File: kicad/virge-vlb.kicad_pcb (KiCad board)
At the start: 4 copper layers, 240.5 x 69.4 mm, 92 parts, among them J1 VLB_slot, J2 VGA, U1 74LS244, U2 27C020, U7 86C325, U8 7404, U9 7408, Y1 14.318MHz

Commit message: changed QFP and ROM footprint
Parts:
- added REF**: PLCC-28_SMD-Socket, Package_LCC:PLCC-28_SMD-Socket, F.Cu at (128.2, 170.0)
- added REF**: PLCC-32_11.4x14.0mm_P1.27mm, Package_LCC:PLCC-32_11.4x14.0mm_P1.27mm, F.Cu at (145.7, 170.3)
- J2: footprint Connector_Dsub:DSUB-15-HD_Female_Horizontal_P2.29x1.98mm_EdgePinOffset8.35mm_Housed_MountingHolesOffset10.89mm -> VLB:DSUB-15_female
- R22: value 33R -> 2 x 33R
- U2: footprint Package_DIP:DIP-32_W15.24mm -> VLB:EEPROM_combo
- U7: footprint Package_QFP:PQFP-208_28x28mm_P0.5mm -> VLB:QFP-208
- moved R6 42.0 mm to (191.2, 132.7)
- moved U2 41.2 mm to (187.4, 130.4), turned to 90 degrees
- moved R7 38.3 mm to (189.7, 112.8), turned to 180 degrees
- moved C9 12.1 mm to (231.2, 118.8)
- moved C20 4.72 mm to (254.2, 130.3)
- moved U7 2.49 mm to (97.6, 115.2)
- moved R46 1.50 mm to (74.8, 130.8)
- moved R48 1.48 mm to (76.8, 130.8)
- moved R47 1.47 mm to (75.8, 127.9)
- moved U1 1.45 mm to (239.2, 122.7), turned to 90 degrees
- moved R22 0.45 mm to (99.2, 96.0)
- moved R21 0.44 mm to (97.2, 96.0)
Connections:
- U1 pad 12: /ISA Bus/R_D4 -> /ISA Bus/R_D7
- U1 pad 14: /ISA Bus/R_D5 -> /ISA Bus/R_D6
- U1 pad 16: /ISA Bus/R_D6 -> /ISA Bus/R_D5
- U1 pad 18: /ISA Bus/R_D7 -> /ISA Bus/R_D4
- U1 pad 2: /ISA Bus/ISA_D7 -> /ISA Bus/ISA_D4
- U1 pad 4: /ISA Bus/ISA_D6 -> /ISA Bus/ISA_D5
- U1 pad 6: /ISA Bus/ISA_D5 -> /ISA Bus/ISA_D6
- U1 pad 8: /ISA Bus/ISA_D4 -> /ISA Bus/ISA_D7
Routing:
- net /ISA Bus/R_D0: track 86.5 -> 28.3 mm, vias 0 -> 1
- net /ISA Bus/R_D1: track 74.5 -> 30.0 mm, vias 0 -> 1
- net /ISA Bus/R_A10: track 14.4 -> 58.6 mm, vias 0 -> 1
- net /ISA Bus/R_A11: track 16.2 -> 52.3 mm, vias 0 -> 1
- net /ISA Bus/R_D2: track 63.2 -> 33.3 mm, vias 0 -> 1
- net /ISA Bus/R_A9: track 27.1 -> 50.9 mm, vias 0 -> 1
- net /ISA Bus/R_D3: track 62.6 -> 39.7 mm, vias 0 -> 1
- net /ISA Bus/R_D4: track 48.9 -> 28.3 mm
- net /ISA Bus/R_A0: track 40.3 -> 60.1 mm, vias 0 -> 2
- net /ISA Bus/R_A14: track 18.9 -> 37.7 mm, vias 0 -> 2
- net /ISA Bus/R_A12: track 36.3 -> 18.9 mm, vias 2 -> 0
- net unconnected-(U2-VPP-Pad1): track 0.00 -> 15.6 mm
- net /ISA Bus/R_A8: track 33.0 -> 48.2 mm, vias 0 -> 2
- net /ISA Bus/R_D5: track 45.4 -> 30.8 mm
- net /ISA Bus/R_A1: track 41.3 -> 55.1 mm, vias 0 -> 2
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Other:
- board text added: "(install R7 if 28 pin is used)"
- board text added: "..!.........!.........!.........!.........!........!"
- board text added: "....,.........!.........!.........!.........!......."
- board text added: "......!.........!.........!.........!.........!....."
- board text added: "1"
- board text added: "10"
- board text added: "110"
- board text added: "120"
- board text added: "130"
- board text added: "140"
- board text added: "150"
- board text added: "20"
- board text added: "30"
- board text added: "40"
- board text added: "50"
- board text added: "60"
- board text added: "70"
- board text added: "80"
- board text added: "90"
- board text added: "Rev 1B"
- board text removed: "(install R54 if 28 pin is used)"
- board text removed: "Rev 1A"

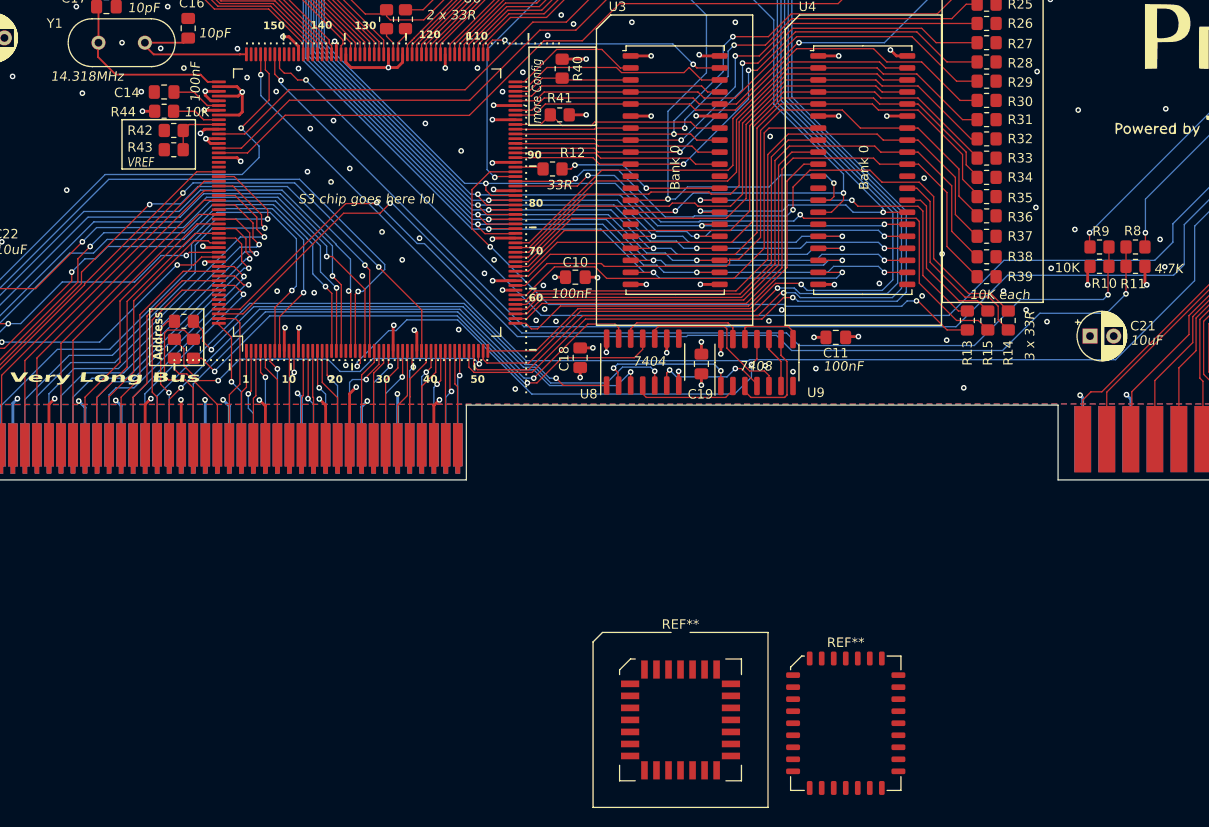
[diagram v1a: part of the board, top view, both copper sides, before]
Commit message: added pull up for VREQ
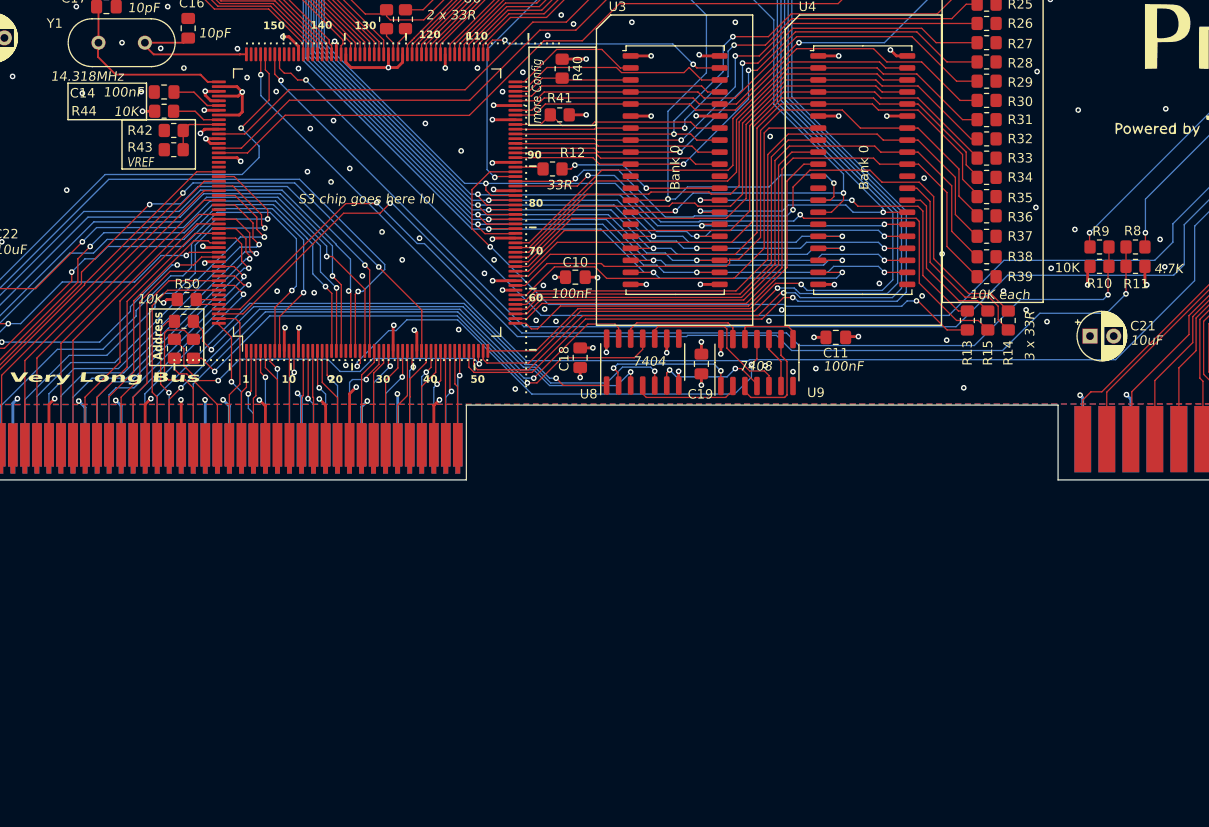
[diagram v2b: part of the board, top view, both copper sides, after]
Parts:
- removed REF**: PLCC-28_SMD-Socket, Package_LCC:PLCC-28_SMD-Socket
- removed REF**: PLCC-32_11.4x14.0mm_P1.27mm, Package_LCC:PLCC-32_11.4x14.0mm_P1.27mm
- added R50: 10K, Resistor_SMD:R_0805_2012Metric_Pad1.20x1.40mm_HandSolder, F.Cu at (76.0, 125.6)
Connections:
- U7 pad 203: unconnected-(U7H-~{VREQ}/VRDY/EVIDEO-Pad203) -> Net-(U7H-~{CREQ}/CRDY/EVCLK)
- U7 pad 204: unconnected-(U7H-~{CREQ}/CRDY/EVCLK-Pad204) -> Net-(U7H-~{CREQ}/CRDY/EVCLK)
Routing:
- net Net-(U7H-~{CREQ}/CRDY/EVCLK): track 0.00 -> 4.99 mm
- net VCC: track 128.2 -> 129.8 mm, vias 46 -> 47
- net /VL Bus/VL_A22: track 21.8 -> 22.6 mm
- net /VL Bus/VL_A18: track 24.8 -> 25.6 mm
- net /VL Bus/VL_A20: track 23.4 -> 24.2 mm

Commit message: some polishing
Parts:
- removed the R43 at (74.7, 109.8)
- added C26: 10uF, Capacitor_SMD:C_1206_3216Metric_Pad1.33x1.80mm_HandSolder, F.Cu at (152.7, 91.0)
- added C27: 10uF, Capacitor_SMD:C_1206_3216Metric_Pad1.33x1.80mm_HandSolder, F.Cu at (59.0, 108.2)
- added C28: 10uF, Capacitor_SMD:C_1206_3216Metric_Pad1.33x1.80mm_HandSolder, F.Cu at (61.0, 81.1)
- added C29: 10uF, Capacitor_SMD:C_1206_3216Metric_Pad1.33x1.80mm_HandSolder, F.Cu at (264.6, 81.2)
- C19: renamed from C15; value 100nF -> 1nF
- C20, C21, C22, C23, C24, C25: footprint Capacitor_THT:CP_Radial_D5.0mm_P2.50mm -> Capacitor_SMD:C_1206_3216Metric_Pad1.33x1.80mm_HandSolder
- moved C22 9.41 mm to (59.0, 115.6)
- moved C24 7.72 mm to (59.0, 91.8)
- moved C23 7.13 mm to (34.5, 131.6)
- moved C9 5.28 mm to (71.5, 94.5), turned to 0 degrees
- moved R41 1.51 mm to (117.0, 106.1)
- moved R40 1.40 mm to (117.0, 101.8), turned to 180 degrees
- moved R44 0.98 mm to (73.7, 107.8)
- moved C25 0.61 mm to (159.3, 84.2), turned to 0 degrees
- moved C10 0.12 mm to (67.6, 94.5)
- renumbered C17 to C10, C19 to C15, C10 to C16, C9 to C17, C16 to C9, R20 to R10, R49 to R11, R22 to R20, R10 to R22, R50 to R42, R44 to R43, R42 to R44, R11 to R46, R46 to R49
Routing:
- net VCC: track 129.8 -> 144.5 mm, vias 47 -> 57
- net GND: track 166.7 -> 164.7 mm, vias 220 -> 221
- net Net-(U7H-RSET): track 6.06 -> 5.02 mm
- net /Memory Bus/PD0: track 14.4 -> 13.5 mm
- net /Memory Bus/PD1: track 12.8 -> 13.5 mm
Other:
- board text added: "- 10K: R22 -> R43 - 33R: R1, R2, R9 -> R22 - 75R: R3, R4, R5 - 4.7K: R8, R46 - 150R: R44 - 100R: R45 - 0R: R6, R7 + address box"
- board text added: "- 10pF: C1 -> C10 - 100nF: C11 -> C18 - 10uF: C20 -> C29 - 1nF: C19"
- board text added: "- U1: 74244 buffer - U2: VBIOS EEPROM - U3, U4, U5, U6: SOJ-40 VRAM - U7: S3 Trio64V+ (86C765) or S3 ViRGE (86C325) - U8: 7404 hex inverter - U9: 7408 quad 2-input AND"
- board text added: "- Y1: 14.318MHz crystal - FP1, FB2, FB3: ferrite beads"
- board text added: "....!.........!.........!.........!.........!......."
- board text added: "........!.........!.........!.........!.........!..."
- board text added: "100"
- board text added: "160"
- board text added: "170"
- board text added: "180"
- board text added: "190"
- board text added: "200"
- board text added: "Capacitors:"
- board text added: "Chips:"
- board text added: "Other:"
- board text added: "Parts list"
- board text added: "Resistors:"
- board text removed: "....,.........!.........!.........!.........!......."
- board text removed: "VREF"
